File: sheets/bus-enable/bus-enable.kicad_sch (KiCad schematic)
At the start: 2 parts, among them U1 4066

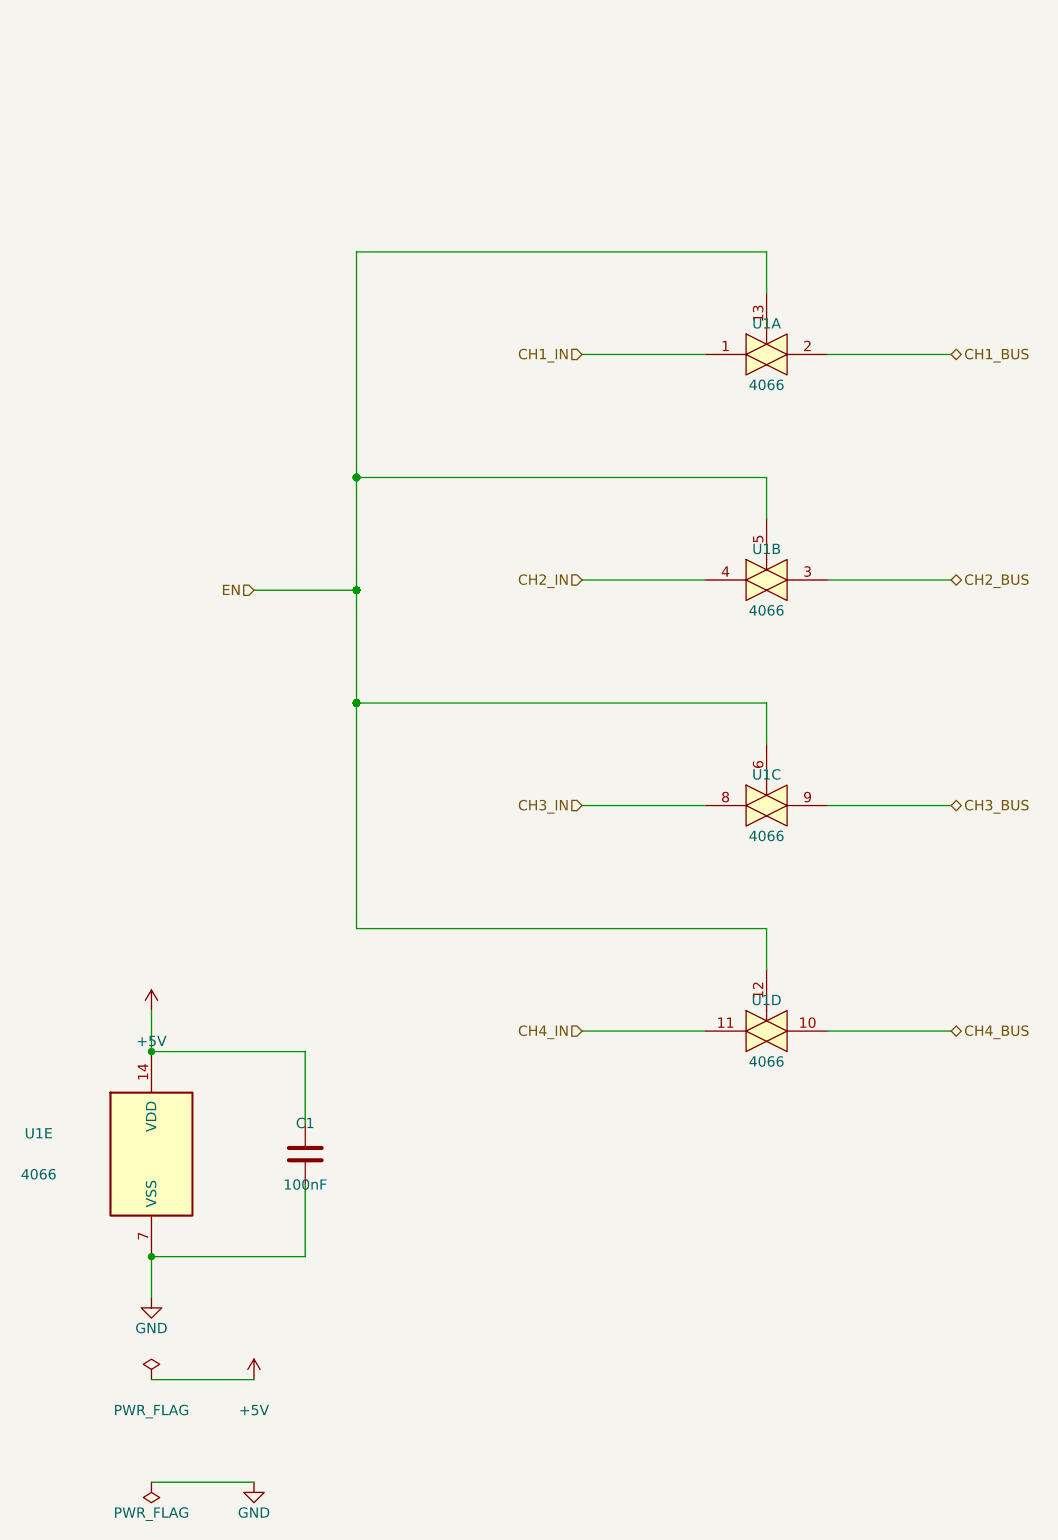
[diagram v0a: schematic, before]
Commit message: Decouple every supply pin
Each integrated circuit now has a 100nF ceramic across its supply pins,
one per package and one per rail for a split supply. Nine capacitors
across five blocks. Home boards are two layers with no ground plane, so
nothing else holds the rail up during a switching edge.

cv-output gains GND as an interface net. It had no ground reference at
all before, being a buffer between the two analogue rails, so the
decoupling brought one in and the harness needed a PWR_FLAG for it.

clock-input 1.1.1, cv-output 1.1.1, step-counter 1.0.1, cv-mux-8 1.0.1,
cv-scale-offset 1.0.1. No circuit change in any of them.

Recorded as a convention in the repo README, next to the footprint and
hierarchical label rules. ERC checks none of these three.

All nine blocks: ERC 0 errors, no overlaps.

Co-Authored-By: Claude Opus 5 (1M context) <noreply@anthropic.com>
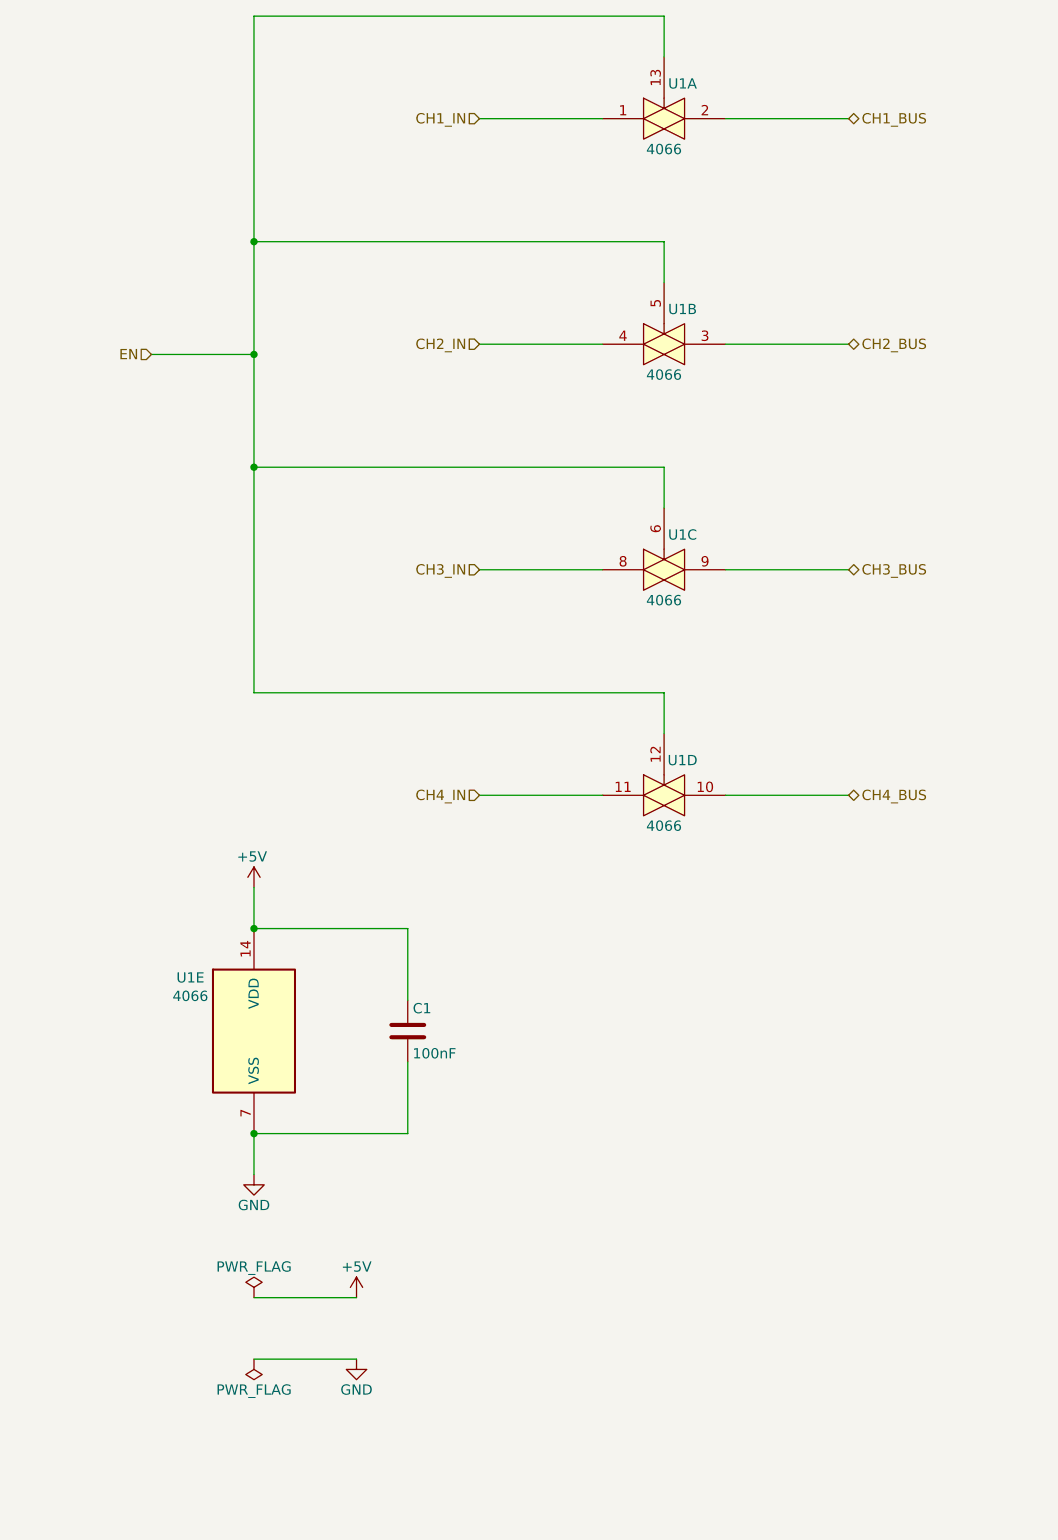
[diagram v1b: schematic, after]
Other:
- moved on the sheet: C1, U1A, U1B, U1C, U1D, U1E
